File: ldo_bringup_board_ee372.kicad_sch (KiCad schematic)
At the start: 81 parts, among them J1 VIN, J10 MD_SW_EN, J13 VSIG, J14 VSIG_BUF, J15 NR, J18 VIN_PROBE, J19 VREF_PROBE, J2 GND, J20 VOUT_PROBE, J3 IBIAS, J4 VOUT, J5 VIN_SMA, J6 VOUT_SMA, J7 GND, J8 5V, Q1 FDV305N, Q2 FDV305N, Q3 FDV305N, Q4 FDV305N, Q5 FDV305N, SW1 MD_SW, U1 LDO_DualMode_BGR_EE372

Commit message: Schematic changes after the freeze: drop 14 test points, add R54, move input caps
The schematic changed after the freeze commit f5ce739. It now has 151
parts and 109 nets. ERC 0 errors.

- Removed TP9 to TP13 and TP15 to TP19 (on VG0 to VG4) and TP22 to TP25
  (on the four shunt nodes)
- Added R54 (0 ohm, 0805, DNP) between the J3 IBIAS jack and the IBIAS
  net at U1 pin 5
- C6, C7, C9 and C11 moved from VDD (SHUNT_IN_A) to VDD_LDO
  (SHUNT_IN_B), the chip side of the R4 shunt
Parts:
- removed TP10: VG1, TestPoint:TestPoint_Keystone_5005-5009_Compact, symbol Connector:TestPoint
- removed TP11: VG2, TestPoint:TestPoint_Keystone_5005-5009_Compact, symbol Connector:TestPoint
- removed TP12: VG3, TestPoint:TestPoint_Keystone_5005-5009_Compact, symbol Connector:TestPoint
- removed TP13: VG4, TestPoint:TestPoint_Keystone_5005-5009_Compact, symbol Connector:TestPoint
- removed TP22: SHUNT_IN_A, TestPoint:TestPoint_Keystone_5005-5009_Compact, symbol Connector:TestPoint
- removed TP23: SHUNT_IN_B, TestPoint:TestPoint_Keystone_5005-5009_Compact, symbol Connector:TestPoint
- removed TP24: SHUNT_OUT_A, TestPoint:TestPoint_Keystone_5005-5009_Compact, symbol Connector:TestPoint
- removed TP25: SHUNT_OUT_B, TestPoint:TestPoint_Keystone_5005-5009_Compact, symbol Connector:TestPoint
- removed TP9: VG0, TestPoint:TestPoint_Keystone_5005-5009_Compact, symbol Connector:TestPoint
- added R54: 0, Resistor_SMD:R_0805_2012Metric_Pad1.20x1.40mm_HandSolder, symbol Device:R
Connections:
- net IBIAS: now also R54.2; no longer J3.1 (Pin_1)
- net SHUNT_IN_B: now also C11.1, C6.1, C7.1, C9.1
- net VDD: no longer C11.1, C6.1, C7.1, C9.1
- new net: J3.1 (Pin_1), R54.1
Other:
- moved on the sheet: J3

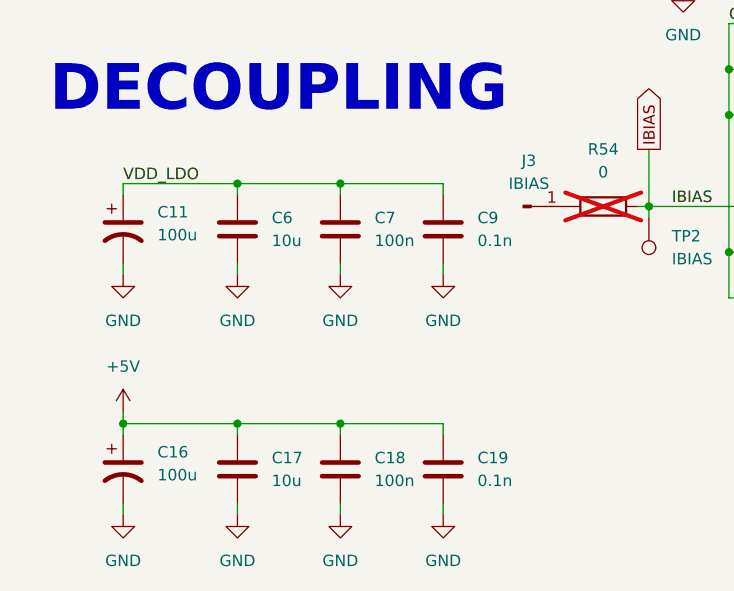
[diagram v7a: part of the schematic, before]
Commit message: Add R55 in series with C11
R55 (0 ohm, 0805, fitted) sits between C11 (100u) and VDD_LDO. Lifting
it takes C11 off the rail that R4 measures. 152 parts, 110 nets, ERC 0
errors.
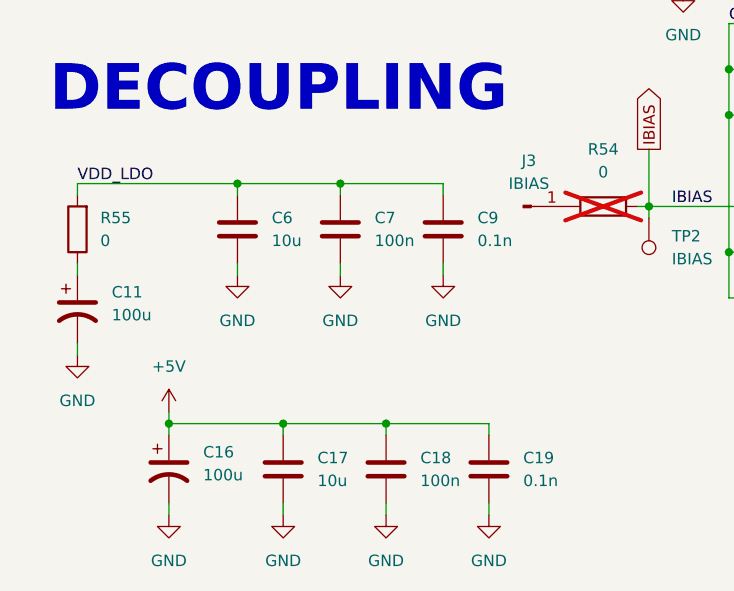
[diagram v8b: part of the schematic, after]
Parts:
- added R55: 0, Resistor_SMD:R_0805_2012Metric_Pad1.20x1.40mm_HandSolder, symbol Device:R
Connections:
- net SHUNT_IN_B: now also R55.2; no longer C11.1
- new net: C11.1, R55.1
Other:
- moved on the sheet: C11, C16, C17, C18, C19
